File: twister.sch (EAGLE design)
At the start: 30 parts, among them IC1 A3967SLB, U1 ARDUINO_SHIELDNOHOLES

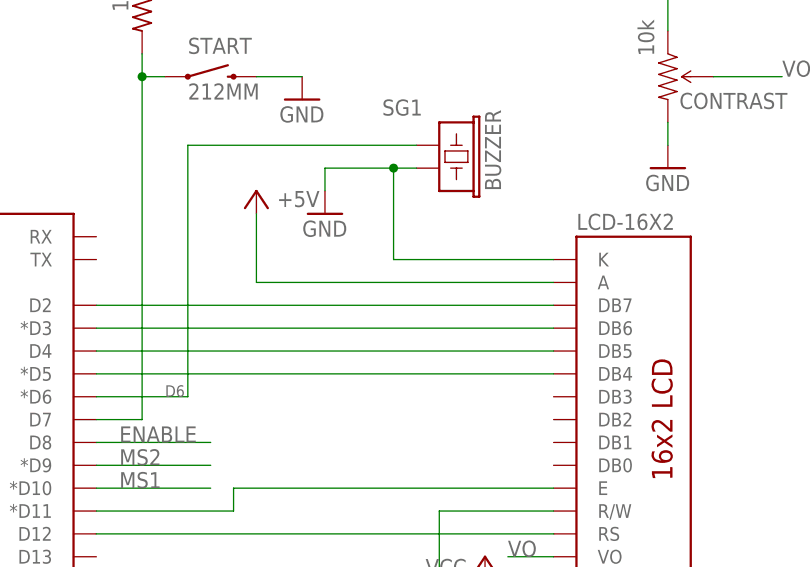
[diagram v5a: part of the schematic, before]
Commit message: Put together first PCB, started documenting improvements.
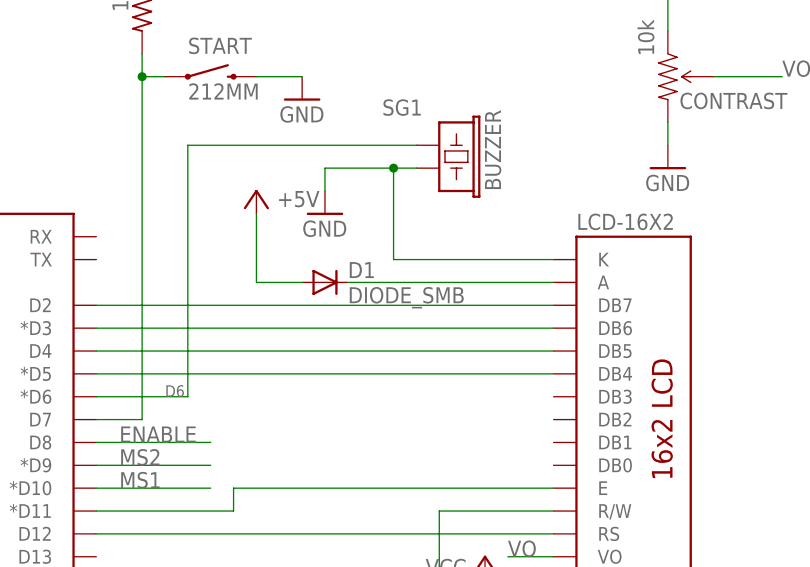
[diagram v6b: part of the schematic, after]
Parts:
- added D1: DIODE_SMB, twister_clean:DIODE_SMB
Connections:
- new net A: D1.C, LCD_MODULE.A
- net +5V: now also D1.A; no longer LCD_MODULE.A
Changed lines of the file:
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@@
 <?xml version="1.0" encoding="utf-8"?>
 <!DOCTYPE eagle SYSTEM "eagle.dtd">
-<eagle version="6.5.0">
+<eagle version="6.4">
 <drawing>
 <settings>
@@
 <part name="P+18" library="twister_clean" deviceset="+5V" device="" value="+5V"/>
 <part name="FRAME2" library="frames" deviceset="DINA3_L" device=""/>
+<part name="D1" library="twister_clean" deviceset="DIODE" device="_SMB"/>
 </parts>
 <sheets>
@@
 <instance part="FRAME2" gate="G$1" x="-53.34" y="-81.28"/>
 <instance part="FRAME2" gate="G$2" x="233.68" y="-81.28"/>
+<instance part="D1" gate="1" x="78.74" y="99.06"/>
 </instances>
 <busses>
@@
 </segment>
 <segment>
-<pinref part="LCD_MODULE" gate="G$1" pin="A"/>
 <pinref part="P+16" gate="1" pin="+5V"/>
-<wire x1="104.14" y1="99.06" x2="71.12" y2="99.06" width="0.1524" layer="91"/>
 <wire x1="71.12" y1="99.06" x2="71.12" y2="106.68" width="0.1524" layer="91"/>
+<pinref part="D1" gate="1" pin="A"/>
+<wire x1="71.12" y1="99.06" x2="76.2" y2="99.06" width="0.1524" layer="91"/>
 </segment>
 <segment>
@@
 </segment>
 </net>
+<net name="A" class="0">
+<segment>
+<pinref part="D1" gate="1" pin="C"/>
+<pinref part="LCD_MODULE" gate="G$1" pin="A"/>
+<wire x1="81.28" y1="99.06" x2="104.14" y2="99.06" width="0.1524" layer="91"/>
+</segment>
+</net>

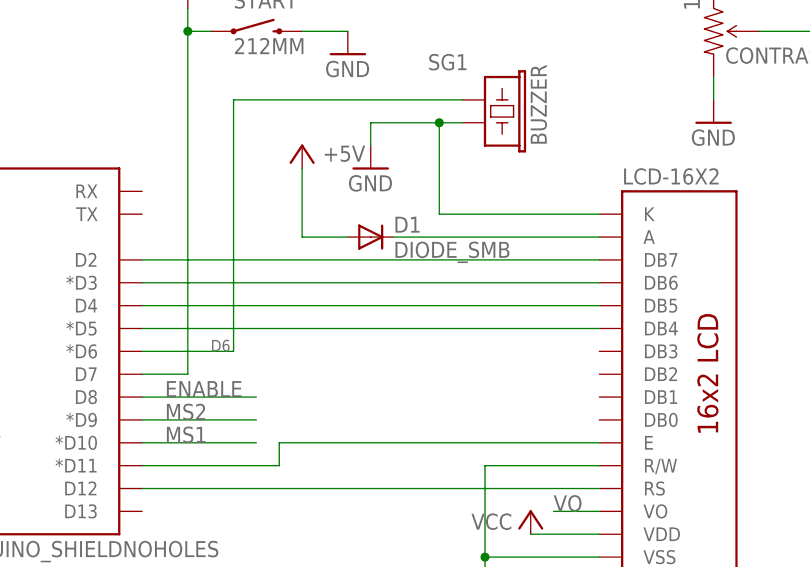
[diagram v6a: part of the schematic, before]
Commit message: Designed a new tetrode holder capable of handling the high speeds of the twister.
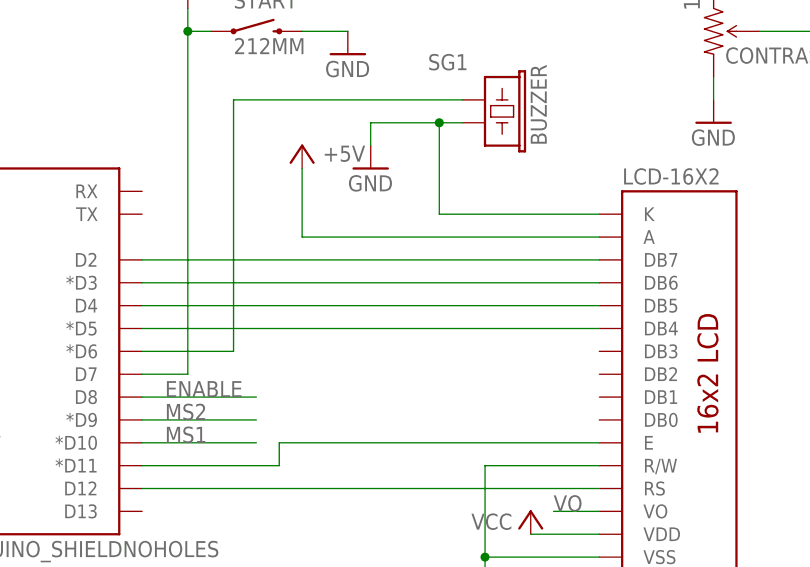
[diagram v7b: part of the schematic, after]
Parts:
- removed D1: DIODE_SMB, twister_clean:DIODE_SMB
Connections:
- removed net A: D1.C, LCD_MODULE.A
- net +5V: now also LCD_MODULE.A; no longer D1.A
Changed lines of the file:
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@@
 <?xml version="1.0" encoding="utf-8"?>
 <!DOCTYPE eagle SYSTEM "eagle.dtd">
-<eagle version="6.4">
+<eagle version="6.5.0">
 <drawing>
 <settings>
@@
 <part name="P+18" library="twister_clean" deviceset="+5V" device="" value="+5V"/>
 <part name="FRAME2" library="frames" deviceset="DINA3_L" device=""/>
-<part name="D1" library="twister_clean" deviceset="DIODE" device="_SMB"/>
 </parts>
 <sheets>
@@
 <instance part="FRAME2" gate="G$1" x="-53.34" y="-81.28"/>
 <instance part="FRAME2" gate="G$2" x="233.68" y="-81.28"/>
-<instance part="D1" gate="1" x="78.74" y="99.06"/>
 </instances>
 <busses>
@@
 </segment>
 <segment>
+<pinref part="LCD_MODULE" gate="G$1" pin="A"/>
 <pinref part="P+16" gate="1" pin="+5V"/>
+<wire x1="104.14" y1="99.06" x2="71.12" y2="99.06" width="0.1524" layer="91"/>
 <wire x1="71.12" y1="99.06" x2="71.12" y2="106.68" width="0.1524" layer="91"/>
-<pinref part="D1" gate="1" pin="A"/>
-<wire x1="71.12" y1="99.06" x2="76.2" y2="99.06" width="0.1524" layer="91"/>
 </segment>
 <segment>
@@
 <segment>
 <wire x1="63.5" y1="114.3" x2="88.9" y2="114.3" width="0.1524" layer="91"/>
-<label x="60.96" y="86.36" size="1.27" layer="95"/>
 <pinref part="BUZZER" gate="G$1" pin="2"/>
 <pinref part="U1" gate="G$1" pin="*D6"/>
@@
 </segment>
 </net>
-<net name="A" class="0">
-<segment>
-<pinref part="D1" gate="1" pin="C"/>
-<pinref part="LCD_MODULE" gate="G$1" pin="A"/>
-<wire x1="81.28" y1="99.06" x2="104.14" y2="99.06" width="0.1524" layer="91"/>
-</segment>
-</net>
